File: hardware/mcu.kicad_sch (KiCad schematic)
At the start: 20 parts, among them J1 UART MCU, SW1 BOOT, SW2 RESET, U15 VEML7700, U3 ESP32-WROVER-E

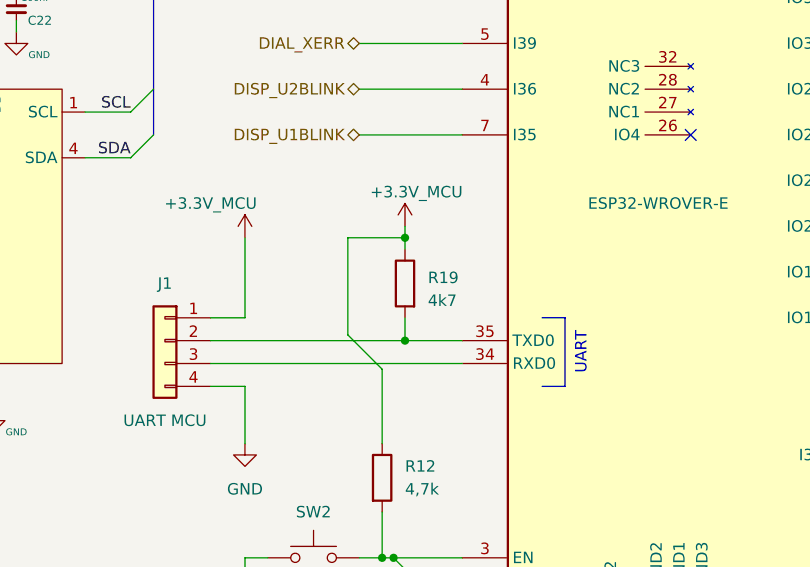
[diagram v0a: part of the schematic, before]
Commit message: Remove R19, pull-up disturbs serial communication
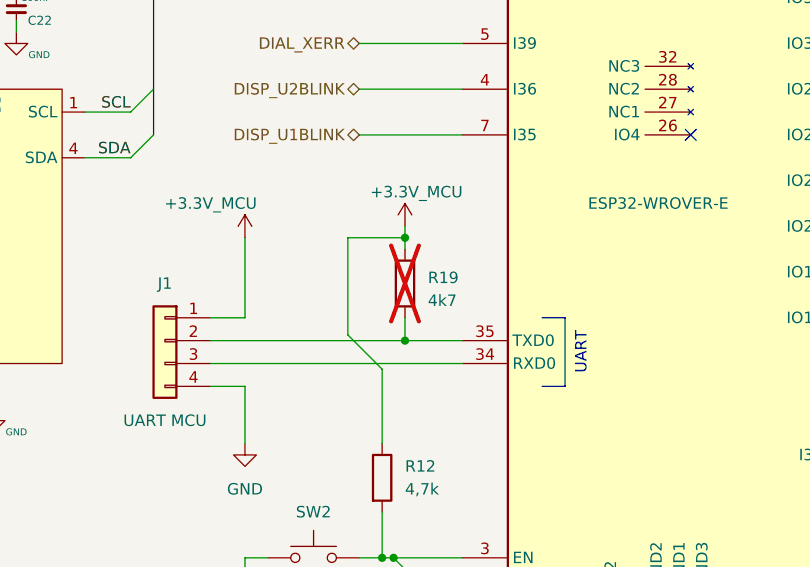
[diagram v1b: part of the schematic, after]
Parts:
- R19: now not fitted
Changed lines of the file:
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@@
 		(in_bom yes)
 		(on_board yes)
-		(dnp no)
+		(dnp yes)
 		(property "Reference" "R19"
 			(at 134.62 111.125 0)

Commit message: Minor design updates
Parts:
- C12: value 1uF -> 1μF
- C13: value 47uF -> 47μF
- R12: value 4,7k -> 4,7kΩ
- R13, R2: value 4.7k -> 4,7kΩ
- R14, R15, R16, R22: value 10k -> 10kΩ
- R17, R18: value 4k7 -> 4,7kΩ
- R19: value 4k7 -> 4,7k
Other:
- moved on the sheet: R17
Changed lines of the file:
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@@
 	)
 	(junction
+		(at 95.25 41.91)
+		(diameter 0)
+		(color 0 0 0 0)
+	)
+	(junction
 		(at 132.08 106.68)
 		(diameter 0)
@@
 	)
 	(junction
-		(at 92.71 41.91)
-		(diameter 0)
-		(color 0 0 0 0)
-	)
-	(junction
 		(at 190.5 130.81)
 		(diameter 0)
@@
 	(wire
 		(pts
-			(xy 77.47 41.91) (xy 92.71 41.91)
+			(xy 77.47 41.91) (xy 95.25 41.91)
 		)
 		(stroke
@@
 	(wire
 		(pts
-			(xy 92.71 39.37) (xy 92.71 41.91)
+			(xy 95.25 39.37) (xy 95.25 41.91)
 		)
 		(stroke
@@
 	(wire
 		(pts
-			(xy 92.71 29.21) (xy 92.71 31.75)
+			(xy 95.25 29.21) (xy 95.25 31.75)
 		)
 		(stroke
@@
 	(wire
 		(pts
-			(xy 92.71 41.91) (xy 101.6 41.91)
-		)
-		(stroke
-			(width 0)
-			(type default)
-		)
-	)
-	(wire
-		(pts
 			(xy 154.94 31.75) (xy 157.48 31.75)
 		)
@@
 		)
 	)
+	(wire
+		(pts
+			(xy 95.25 41.91) (xy 101.6 41.91)
+		)
+		(stroke
+			(width 0)
+			(type default)
+		)
+	)
 	(polyline
 		(pts
@@
 			)
 		)
-		(property "Value" "4k7"
+		(property "Value" "4,7kΩ"
 			(at 81.28 37.465 0)
 			(effects
@@
 	(symbol
 		(lib_id "power_espena:+3.3V_MCU")
-		(at 92.71 29.21 0)
+		(at 95.25 29.21 0)
 		(unit 1)
 		(exclude_from_sim no)
@@
 		(dnp no)
 		(property "Reference" "#PWR04"
-			(at 92.71 33.02 0)
+			(at 95.25 33.02 0)
 			(effects
 				(font
@@
 		)
 		(property "Value" "+3.3V_MCU"
-			(at 95.25 24.13 0)
+			(at 97.79 24.13 0)
 			(effects
 				(font
@@
 		)
 		(property "Footprint" ""
-			(at 92.71 29.21 0)
+			(at 95.25 29.21 0)
 			(effects
 				(font
@@
 		)
 		(property "Datasheet" ""
-			(at 92.71 29.21 0)
+			(at 95.25 29.21 0)
 			(effects
 				(font
@@
 		)
 		(property "Description" "Power symbol creates a global label with name \"+3.3V_MCU\""
-			(at 92.71 29.21 0)
+			(at 95.25 29.21 0)
 			(effects
 				(font
@@
 			)
 		)
-		(property "Value" "10k"
+		(property "Value" "10kΩ"
 			(at 152.4 158.115 0)
 			(effects
@@
 			)
 		)
-		(property "Value" "10k"
+		(property "Value" "10kΩ"
 			(at 189.23 66.675 0)
 			(effects
@@
 			)
 		)
-		(property "Value" "10k"
+		(property "Value" "10kΩ"
 			(at 189.23 137.795 0)
 			(effects
@@
 			)
 		)
-		(property "Value" "10k"
+		(property "Value" "10kΩ"
 			(at 189.23 122.555 0)
 			(effects
@@
 	(symbol
 		(lib_id "Device:R")
-		(at 92.71 35.56 0)
+		(at 95.25 35.56 0)
 		(unit 1)
 		(exclude_from_sim no)
@@
 		(dnp yes)
 		(property "Reference" "R17"
-			(at 90.17 34.925 0)
+			(at 92.71 34.925 0)
 			(effects
 				(font
@@
 			)
 		)
-		(property "Value" "4k7"
-			(at 90.17 37.465 0)
+		(property "Value" "4,7kΩ"
+			(at 92.71 37.465 0)
 			(effects
 				(font
@@
 		)
 		(property "Footprint" "Resistor_SMD:R_0805_2012Metric"
-			(at 90.932 35.56 90)
+			(at 93.472 35.56 90)
 			(effects
 				(font
@@
 		)
 		(property "Datasheet" "~"
-			(at 92.71 35.56 0)
+			(at 95.25 35.56 0)
 			(effects
 				(font
@@
 		)
 		(property "Description" "Resistor"
-			(at 92.71 35.56 0)
+			(at 95.25 35.56 0)
 			(effects
 				(font
@@
 			)
 		)
-		(property "Value" "47uF"
+		(property "Value" "47μF"
 			(at 161.29 33.02 0)
 			(effects
@@
 			)
 		)
-		(property "Value" "4.7k"
+		(property "Value" "4,7kΩ"
 			(at 191.77 39.3699 0)
 			(effects
@@
 			)
 		)
-		(property "Value" "4.7k"
+		(property "Value" "4,7kΩ"
 			(at 130.81 40.005 0)
 			(effects
@@
 			)
 		)
-		(property "Value" "1uF"
+		(property "Value" "1μF"
 			(at 128.27 150.495 0)
 			(effects
@@
 			)
 		)
-		(property "Value" "4,7k"
+		(property "Value" "4,7kΩ"
 			(at 132.08 134.6199 0)
 			(effects
@@
 			)
 		)
-		(property "Value" "4k7"
+		(property "Value" "4,7k"
 			(at 134.62 113.665 0)
 			(effects
